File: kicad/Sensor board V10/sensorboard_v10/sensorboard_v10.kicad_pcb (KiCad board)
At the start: 2 copper layers, 100 x 100 mm, 88 parts, among them J1 Conn_01x02, J10 Conn_01x04, J11 Conn_01x02, J12 Conn_01x03, J13 Conn_01x03, J14 Conn_01x03, J15 Conn_01x03, J16 Conn_01x03, J17 Conn_01x03, J18 Conn_01x03, J19 Conn_01x03, J2 USB_C_Receptacle_USB2.0_14P, J3 Conn_01x02, J4 Conn_01x02, J5 Conn_01x02, J6 Conn_01x04, J7 Conn_01x04, J8 Conn_01x02, J9 Conn_01x02, Q1 MMBT3904, Q2 MMBT3904, SW1 SW_SPST, SW2 SW_SPST, U1 ESP32-S3-WROOM-2, U2 CH340C, U3 TJA1051T-3, U4 LM2576S-5, U5 AMS1117-3.3, U6 LM324

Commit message: Sensor Board V10 schematics
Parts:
- added C22: 100nF, RMC_Capacitor:C_0805_2012Metric_Pad1.18x1.45mm_HandSolder_L, F.Cu at (128.0, 121.8)
- added C23: 100nF, RMC_Capacitor:C_0805_2012Metric_Pad1.18x1.45mm_HandSolder_L, F.Cu at (131.0, 121.8)
- added C24: 100nF, RMC_Capacitor:C_0805_2012Metric_Pad1.18x1.45mm_HandSolder_L, F.Cu at (134.0, 121.8)
- added C25: 100nF, RMC_Capacitor:C_0805_2012Metric_Pad1.18x1.45mm_HandSolder_L, F.Cu at (137.0, 121.8)
- added C26: 100nF, RMC_Capacitor:C_0805_2012Metric_Pad1.18x1.45mm_HandSolder_L, F.Cu at (260.8, 122.8)
- added C27: 100nF, RMC_Capacitor:C_0805_2012Metric_Pad1.18x1.45mm_HandSolder_L, F.Cu at (260.8, 125.8)
- added C28: 100nF, RMC_Capacitor:C_0805_2012Metric_Pad1.18x1.45mm_HandSolder_L, F.Cu at (202.0, 111.8)
- added C29: 100nF, RMC_Capacitor:C_0805_2012Metric_Pad1.18x1.45mm_HandSolder_L, F.Cu at (107.0, 86.2)
- added D3: LED, RMC_LED:LED_0805_2012Metric_Pad1.45x1.40mm_HandSolder, F.Cu at (229.8, 71.8)
- added D4: LED, RMC_LED:LED_0805_2012Metric_Pad1.45x1.40mm_HandSolder, F.Cu at (229.8, 74.8)
- added J20: Conn_01x02, Connector_JST:JST_XH_B2B-XH-A_1x02_P2.50mm_Vertical, F.Cu at (196.0, 107.0)
- added J21: Conn_01x06, Connector_PinHeader_2.54mm:PinHeader_2x03_P2.54mm_Vertical, F.Cu at (237.8, 51.5)
- added R30: 5k, RMC_Resistor:R_0805_2012Metric_Pad1.20x1.40mm_HandSolder_L, F.Cu at (128.0, 127.2)
- added R31: 1k, RMC_Resistor:R_0805_2012Metric_Pad1.20x1.40mm_HandSolder_L, F.Cu at (130.9, 127.2)
- added R32: 5k, RMC_Resistor:R_0805_2012Metric_Pad1.20x1.40mm_HandSolder_L, F.Cu at (133.9, 127.2)
- added R33: 1k, RMC_Resistor:R_0805_2012Metric_Pad1.20x1.40mm_HandSolder_L, F.Cu at (136.8, 127.2)
- added R34: 5k, RMC_Resistor:R_0805_2012Metric_Pad1.20x1.40mm_HandSolder_L, F.Cu at (139.8, 127.2)
- added R35: 1k, RMC_Resistor:R_0805_2012Metric_Pad1.20x1.40mm_HandSolder_L, F.Cu at (142.7, 127.2)
- added R36: 4k7, RMC_Resistor:R_0805_2012Metric_Pad1.20x1.40mm_HandSolder_L, F.Cu at (260.7, 128.7)
- added R37: 100K, RMC_Resistor:R_0805_2012Metric_Pad1.20x1.40mm_HandSolder_L, F.Cu at (202.0, 117.7)
- added R38: 330R, RMC_Resistor:R_0805_2012Metric_Pad1.20x1.40mm_HandSolder_L, F.Cu at (222.1, 69.6)
- added R39: 120R, RMC_Resistor:R_0805_2012Metric_Pad1.20x1.40mm_HandSolder_L, F.Cu at (222.1, 72.6)
- added U7: TXS0102DCU, Package_SO:VSSOP-8_2.3x2mm_P0.5mm, F.Cu at (52.0, 118.0)
- R24, R25, R26, R27: footprint RMC_Resistor:R_0805_2012Metric_Pad1.20x1.40mm_HandSolder_L -> RMC_Resistor:R_1206_3216Metric_Pad1.30x1.75mm_HandSolder_RMC
- U1: footprint RF_Module:ESP32-S3-WROOM-2 -> to be sorted:ESP32-WROOM-S3-2
- U2: footprint Package_SO:SOIC-16_3.9x9.9mm_P1.27mm -> RMC_SO:SOIC-16_3.9x9.9mm_P1.27mm_Handsolder
- moved R21 209.1 mm to (222.3, 144.7)
- moved R22 209.1 mm to (222.3, 147.6)
- moved C20 209.1 mm to (227.7, 144.7)
- moved J19 209.1 mm to (223.0, 138.8)
- moved C17 188.6 mm to (230.0, 120.4)
- moved J16 188.6 mm to (225.2, 114.5)
- moved R15 188.6 mm to (224.5, 120.4)
- moved R16 188.6 mm to (224.5, 123.4)
- moved C3 136.7 mm to (183.8, 64.2)
- moved R24 122.7 mm to (133.6, 134.8), turned to 90 degrees
- moved J4 120.4 mm to (135.5, 143.5), turned to 90 degrees
- moved R25 118.5 mm to (136.5, 134.8), turned to 90 degrees
- moved R26 114.4 mm to (139.5, 134.8), turned to 90 degrees
- moved R27 110.2 mm to (142.5, 134.8), turned to 90 degrees
- moved J5 109.4 mm to (143.3, 143.5), turned to 90 degrees
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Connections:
- net /voltage divider/3.3V_INPUT renamed POT1_IN
- net /voltage divider1/3.3V_INPUT renamed POT2_IN
- net /voltage divider2/3.3V_INPUT renamed POT3_IN
- net /voltage divider3/3.3V_INPUT renamed POT4_IN
- net /voltage divider4/3.3V_INPUT renamed APPS_5V_IN
- net /voltage divider5/3.3V_INPUT renamed BRAKE_IN
- net /voltage divider6/3.3V_INPUT renamed FLOW_IN
- C13 pad 2: /voltage divider/1.65V OUTPUT -> POT1_OUT
- C14 pad 2: /voltage divider1/1.65V OUTPUT -> POT2_OUT
- C15 pad 2: /voltage divider2/1.65V OUTPUT -> POT3_OUT
- C16 pad 2: /voltage divider3/1.65V OUTPUT -> POT4_OUT
- C17 pad 2: /voltage divider4/1.65V OUTPUT -> APPS_5V_OUT
- C18 pad 2: /voltage divider5/1.65V OUTPUT -> BRAKE_OUT
- C19 pad 2: /voltage divider6/1.65V OUTPUT -> FLOW_OUT
- J19 pad 3: +5V -> +3.3V
- R10 pad 2: /voltage divider1/1.65V OUTPUT -> POT2_OUT
- R11 pad 2: /voltage divider2/1.65V OUTPUT -> POT3_OUT
- R12 pad 2: /voltage divider2/1.65V OUTPUT -> POT3_OUT
- R13 pad 2: /voltage divider3/1.65V OUTPUT -> POT4_OUT
- R14 pad 2: /voltage divider3/1.65V OUTPUT -> POT4_OUT
- R15 pad 2: /voltage divider4/1.65V OUTPUT -> APPS_5V_OUT
- R16 pad 2: /voltage divider4/1.65V OUTPUT -> APPS_5V_OUT
- R17 pad 2: /voltage divider5/1.65V OUTPUT -> BRAKE_OUT
- R18 pad 2: /voltage divider5/1.65V OUTPUT -> BRAKE_OUT
- R19 pad 2: /voltage divider6/1.65V OUTPUT -> FLOW_OUT
- R20 pad 2: /voltage divider6/1.65V OUTPUT -> FLOW_OUT
- R7 pad 2: /voltage divider/1.65V OUTPUT -> POT1_OUT
- R8 pad 2: /voltage divider/1.65V OUTPUT -> POT1_OUT
- R9 pad 2: /voltage divider1/1.65V OUTPUT -> POT2_OUT
- U1 pad 10: unconnected-(U1-IO17-Pad10) -> BRAKE_TEMP_OUT3
- U1 pad 11: unconnected-(U1-IO18-Pad11) -> BRAKE_TEMP_OUT4
- U1 pad 12: unconnected-(U1-IO8-Pad12) -> BRAKE_OUT
- U1 pad 13: unconnected-(U1-USB_D-/IO19-Pad13) -> CAN_RX
- U1 pad 14: unconnected-(U1-USB_D+/IO20-Pad14) -> CAN_TX
- U1 pad 15: LVB_S -> LVB_TEMP
- U1 pad 17: unconnected-(U1-IO9-Pad17) -> PUMP_THERMISTOR_IN
- U1 pad 18: unconnected-(U1-IO10-Pad18) -> LVB_S
- U1 pad 19: unconnected-(U1-IO11-Pad19) -> MOSI
- U1 pad 20: unconnected-(U1-IO12-Pad20) -> SCK
- U1 pad 21: unconnected-(U1-IO13-Pad21) -> MISO
- U1 pad 22: unconnected-(U1-IO14-Pad22) -> FLOW_OUT
- U1 pad 23: unconnected-(U1-IO21-Pad23) -> SDA
- U1 pad 31: unconnected-(U1-IO38-Pad31) -> SCL
- U1 pad 8: unconnected-(U1-IO15-Pad8) -> BRAKE_TEMP_OUT1
- U1 pad 9: unconnected-(U1-IO16-Pad9) -> BRAKE_TEMP_OUT2
- U6 pad 13: BRAKE_TEMP_OUT4 -> Net-(U6D--)
- U6 pad 6: BRAKE_TEMP_OUT3 -> Net-(U6B--)
- U6 pad 9: BRAKE_TEMP_OUT2 -> Net-(U6C--)

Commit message: Sensor Board v10
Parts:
- removed J1: Conn_01x02, Connector_JST:JST_VH_B2P-VH_1x02_P3.96mm_Vertical
- added C30: 100nF, RMC_Capacitor:C_0805_2012Metric_Pad1.18x1.45mm_HandSolder_L, B.Cu at (183.2, 131.6)
- added C31: 100nF, RMC_Capacitor:C_0805_2012Metric_Pad1.18x1.45mm_HandSolder_L, B.Cu at (188.1, 135.4)
- added C32: 22uF, RMC_Capacitor:C_0805_2012Metric_Pad1.18x1.45mm_HandSolder_L, F.Cu at (126.2, 143.0)
- added C33: 22uF, RMC_Capacitor:C_0805_2012Metric_Pad1.18x1.45mm_HandSolder_L, F.Cu at (116.2, 143.0)
- added C34: 100nF, RMC_Capacitor:C_0805_2012Metric_Pad1.18x1.45mm_HandSolder_L, F.Cu at (129.6, 143.0)
- added C35: 100nF, RMC_Capacitor:C_0805_2012Metric_Pad1.18x1.45mm_HandSolder_L, F.Cu at (113.4, 143.0)
- added D5: SMA Diode, Diode_SMD:D_SMA_Handsoldering, F.Cu at (107.6, 134.4)
- added J22: Conn_01x02, Connector_JST:JST_XH_B2B-XH-A_1x02_P2.50mm_Vertical, F.Cu at (151.3, 144.3)
- added J23: Conn_01x03, Connector_JST:JST_XH_B3B-XH-A_1x03_P2.50mm_Vertical, F.Cu at (191.7, 106.3)
- added J24: Conn_01x01, Connector_PinHeader_2.54mm:PinHeader_1x01_P2.54mm_Vertical, F.Cu at (158.0, 82.4)
- added J25: Conn_01x04, Connector_JST:JST_XH_B4B-XH-A_1x04_P2.50mm_Vertical, F.Cu at (189.2, 91.7)
- added J26: Conn_01x03, Connector_JST:JST_XH_B3B-XH-A_1x03_P2.50mm_Vertical, F.Cu at (158.2, 141.8)
- added J27: Conn_01x03, Connector_JST:JST_XH_B3B-XH-A_1x03_P2.50mm_Vertical, F.Cu at (165.2, 141.9)
- added L2: 4.7-22uH, RMC_Inductor:L_10.4x10.4_H4.8, F.Cu at (121.0, 134.4)
- added R40: 4k7, RMC_Resistor:R_0805_2012Metric_Pad1.20x1.40mm_HandSolder_L, B.Cu at (154.7, 145.7)
- added R41: 5k1, RMC_Resistor:R_0805_2012Metric_Pad1.20x1.40mm_HandSolder_L, B.Cu at (196.2, 68.6)
- added R42: 5k1, RMC_Resistor:R_0805_2012Metric_Pad1.20x1.40mm_HandSolder_L, B.Cu at (196.2, 65.6)
- added R43: 499R, RMC_Resistor:R_0805_2012Metric_Pad1.20x1.40mm_HandSolder_L, F.Cu at (181.8, 64.0)
- added R44: 680R, RMC_Resistor:R_0805_2012Metric_Pad1.20x1.40mm_HandSolder_L, F.Cu at (123.6, 148.0)
- added U8: 74LVC1G17, Package_TO_SOT_SMD:SOT-23-5_HandSoldering, B.Cu at (182.4, 134.8)
- added U9: MT3608/SDB628, Package_TO_SOT_SMD:SOT-23-6_Handsoldering, F.Cu at (121.0, 143.2)
- C17, C20, C3, R1, R10, R11, R12, R13, R14, R15, R16, R17, R18, R19, R2, R20, R21, R22, R24, R25, R26, R27, R3, R37, R7, R8, R9: moved to B.Cu
- C2: moved to F.Cu
- J21: value Conn_01x06 -> Conn_01x02; footprint Connector_PinHeader_2.54mm:PinHeader_2x03_P2.54mm_Vertical -> Connector_JST:JST_XH_B2B-XH-A_1x02_P2.50mm_Vertical
- R23: value 499R -> 249k
- moved R23 153.3 mm to (118.2, 148.0)
- moved R1 136.0 mm to (162.3, 145.7), turned to 90 degrees
- moved C27 118.6 mm to (145.3, 98.7), turned to 180 degrees
- moved C26 118.5 mm to (145.3, 96.1)
- moved J10 111.5 mm to (150.6, 118.2)
- moved J6 111.5 mm to (150.6, 103.6)
- moved J7 111.5 mm to (150.6, 110.9)
- moved R36 106.1 mm to (159.4, 97.4)
- moved U7 102.5 mm to (152.5, 97.7), turned to 180 degrees
- moved C20 100.4 mm to (171.6, 61.4)
- moved D3 99.0 mm to (131.2, 80.4), turned to 180 degrees
- moved R38 91.3 mm to (131.2, 78.2), turned to 180 degrees
- moved J18 87.7 mm to (185.9, 141.8), turned to -90 degrees
- moved R20 87.1 mm to (188.1, 137.7), turned to 180 degrees
- moved C17 85.0 mm to (171.6, 58.6)
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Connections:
- C28 pad 1: PUMP_THERMISTOR_IN -> PUMP_THERM_IN
- J2 pad A5: unconnected-(J2-CC1-PadA5) -> Net-(J2-CC1)
- J2 pad B5: unconnected-(J2-CC2-PadB5) -> Net-(J2-CC2)
- J20 pad 1: PUMP_THERMISTOR_IN -> PUMP_THERM_IN
- J21 pad 1: MISO -> CAN+
- J21 pad 2: +5V -> CAN-
- J4 pad 1: GND -> BRAKE_TEMP1
- J4 pad 2: BRAKE_TEMP1 -> +24V
- J5 pad 1: GND -> BRAKE_TEMP2
- J5 pad 2: BRAKE_TEMP2 -> +24V
- J8 pad 1: GND -> BRAKE_TEMP3
- J8 pad 2: BRAKE_TEMP3 -> +24V
- J9 pad 1: GND -> BRAKE_TEMP4
- J9 pad 2: BRAKE_TEMP4 -> +24V
- R19 pad 2: FLOW_OUT -> Net-(C31-Pad2)
- R20 pad 2: FLOW_OUT -> Net-(C31-Pad2)
- R23 pad 1: USB_RX -> +24V
- R23 pad 2: Net-(U1-TXD0/IO43) -> Net-(U9-FB)
- R24 pad 1: GND -> GND2
- R25 pad 1: GND -> GND2
- R26 pad 1: GND -> GND2
- R27 pad 1: GND -> GND2
- R28 pad 1: Net-(U6A--) -> Net-(U6B--)
- R29 pad 2: Net-(U6A--) -> Net-(U6B--)
- R30 pad 1: Net-(U6C--) -> Net-(U6A--)
- R31 pad 2: Net-(U6C--) -> Net-(U6A--)
- R32 pad 1: Net-(U6B--) -> Net-(U6D--)
- R33 pad 2: Net-(U6B--) -> Net-(U6D--)
- R34 pad 1: Net-(U6D--) -> Net-(U6C--)
- R35 pad 2: Net-(U6D--) -> Net-(U6C--)
- R37 pad 1: PUMP_THERMISTOR_IN -> PUMP_THERM_IN
- U1 pad 12: BRAKE_OUT -> SDA_3V3
- U1 pad 13: CAN_RX -> IO19
- U1 pad 14: CAN_TX -> IO20
- U1 pad 15: LVB_TEMP -> Temp_sensor
- U1 pad 16: unconnected-(U1-IO46-Pad16) -> IO46
- U1 pad 17: PUMP_THERMISTOR_IN -> SCL_3V3
- U1 pad 19: MOSI -> LVB_TEMP
- U1 pad 20: SCK -> BRAKE_OUT
- U1 pad 21: MISO -> PUMP_THERM_IN
- U1 pad 23: SDA -> CAN_RX
- U1 pad 24: unconnected-(U1-IO47-Pad24) -> IO47
- U1 pad 25: unconnected-(U1-IO48-Pad25) -> IO48
- U1 pad 26: unconnected-(U1-IO45-Pad26) -> IO45
- U1 pad 31: SCL -> CAN_TX
- U1 pad 32: unconnected-(U1-MTCK/IO39-Pad32) -> IO39
- U1 pad 33: unconnected-(U1-MTDO/IO40-Pad33) -> IO40
- U1 pad 34: unconnected-(U1-MTDI/IO41-Pad34) -> IO41
- U1 pad 35: unconnected-(U1-MTMS/IO42-Pad35) -> IO42
- U1 pad 37: Net-(U1-TXD0/IO43) -> USB_RX
- U2 pad 3: USB_RX -> Net-(U2-RXD)
- U6 pad 1: BRAKE_TEMP_OUT1 -> BRAKE_TEMP_OUT2
- U6 pad 10: BRAKE_TEMP2 -> BRAKE_TEMP4
- U6 pad 12: BRAKE_TEMP4 -> BRAKE_TEMP3
- U6 pad 14: BRAKE_TEMP_OUT4 -> BRAKE_TEMP_OUT3
- U6 pad 3: BRAKE_TEMP1 -> BRAKE_TEMP2
- U6 pad 5: BRAKE_TEMP3 -> BRAKE_TEMP1
- U6 pad 7: BRAKE_TEMP_OUT3 -> BRAKE_TEMP_OUT1
- U6 pad 8: BRAKE_TEMP_OUT2 -> BRAKE_TEMP_OUT4
- U7 pad 1: SDA -> SCL
- U7 pad 4: SDA_3V3 -> SCL_3V3
- U7 pad 5: SCL_3V3 -> SDA_3V3
- U7 pad 8: SCL -> SDA
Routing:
- net +24V: track 0.00 -> 54.9 mm
- net BRAKE_TEMP4: track 0.00 -> 37.1 mm
- net BRAKE_TEMP3: track 0.00 -> 32.3 mm
- net BRAKE_TEMP1: track 0.00 -> 29.5 mm
- net BRAKE_TEMP2: track 0.00 -> 27.1 mm
- net BRAKE_TEMP_OUT3: track 0.00 -> 22.0 mm
- net BRAKE_TEMP_OUT1: track 0.00 -> 20.9 mm
- net POT3_OUT: track 0.00 -> 20.1 mm
- net POT1_OUT: track 0.00 -> 18.8 mm
- net +12V: track 26.1 -> 44.7 mm
- net BRAKE_TEMP_OUT4: track 0.00 -> 16.5 mm
- net BRAKE_TEMP_OUT2: track 0.00 -> 15.7 mm
- net Net-(D5-K): track 0.00 -> 15.3 mm
- net POT4_OUT: track 0.00 -> 14.9 mm
- net POT2_OUT: track 0.00 -> 13.6 mm
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- added copper zone on B.Cu, net GND2
- added copper zone on F.Cu, net GND2

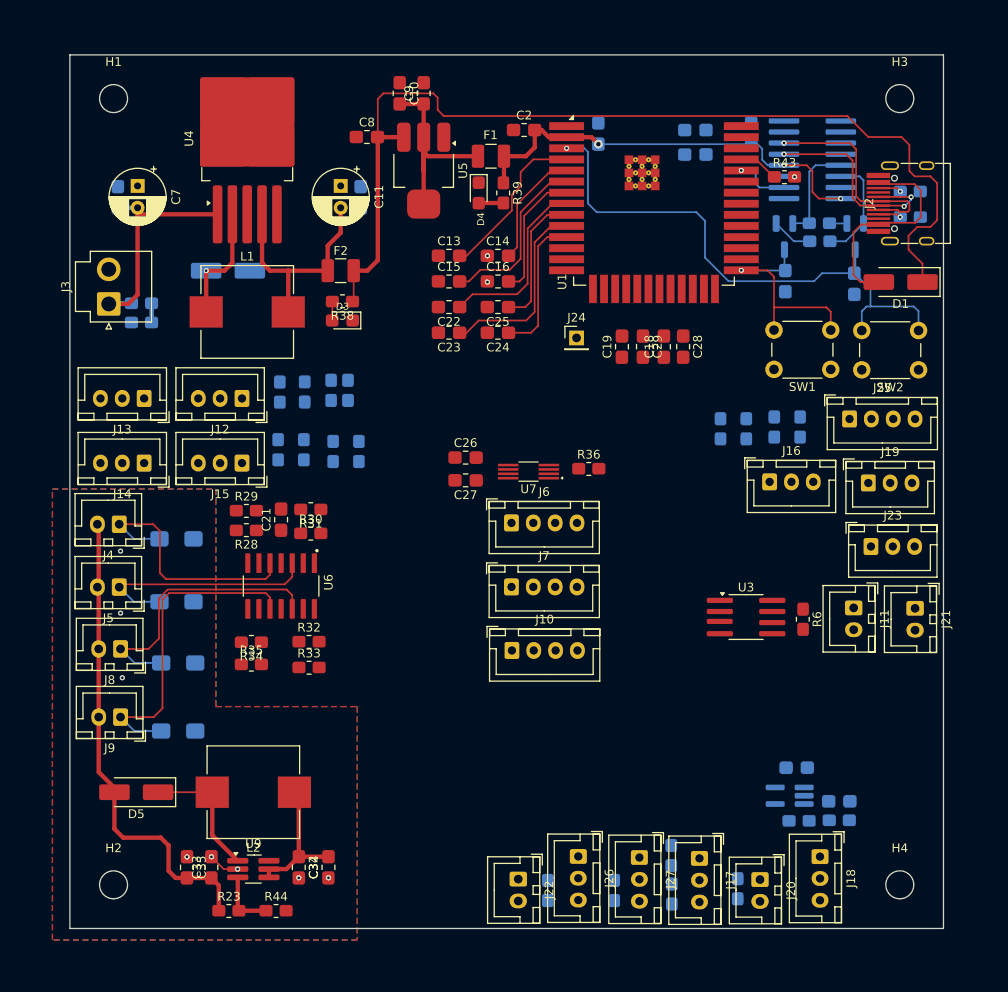
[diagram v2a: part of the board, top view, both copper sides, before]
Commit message: Sensor Board V10.0 done
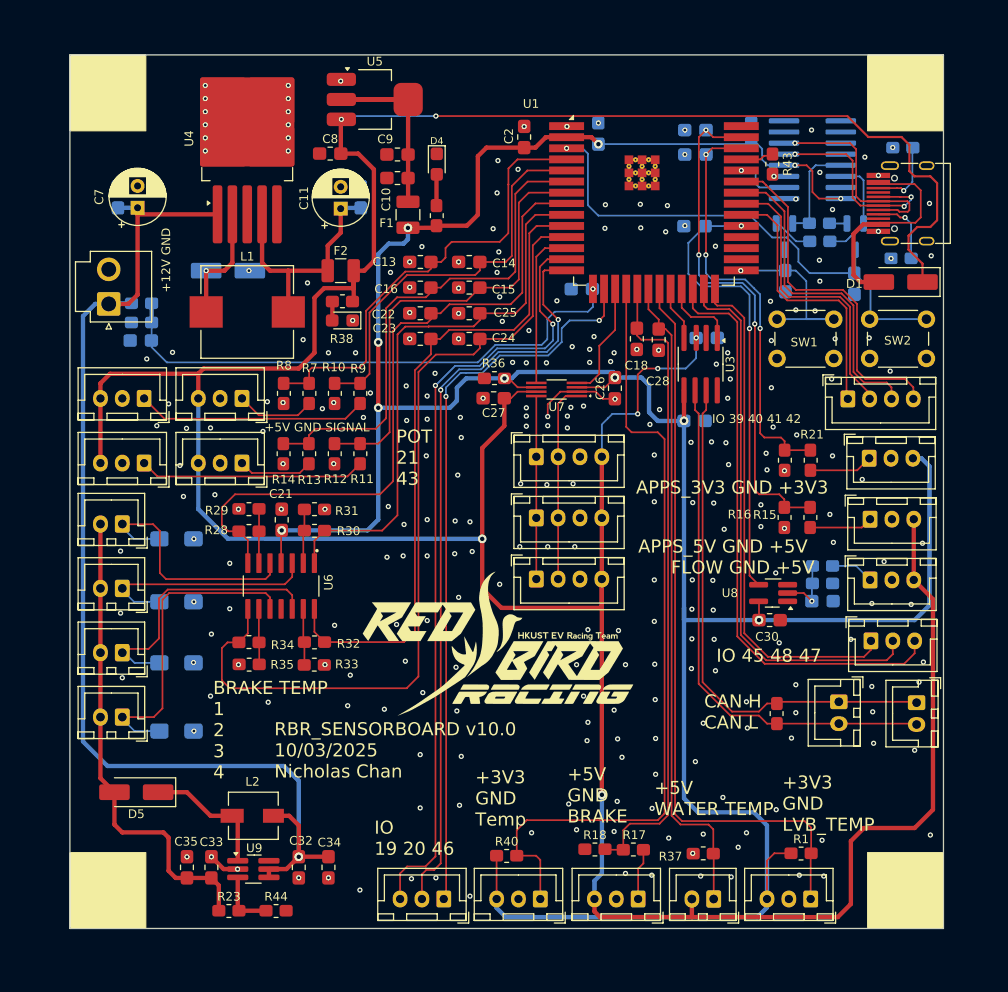
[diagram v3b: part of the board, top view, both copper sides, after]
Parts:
- removed J22: Conn_01x02, Connector_JST:JST_XH_B2B-XH-A_1x02_P2.50mm_Vertical
- removed J24: Conn_01x01, Connector_PinHeader_2.54mm:PinHeader_1x01_P2.54mm_Vertical
- added C36: 100nF, RMC_Capacitor:C_0805_2012Metric_Pad1.18x1.45mm_HandSolder_L, B.Cu at (172.9, 82.4)
- added C37: 100nF, RMC_Capacitor:C_0805_2012Metric_Pad1.18x1.45mm_HandSolder_L, B.Cu at (171.5, 91.9)
- added C38: 100nF, RMC_Capacitor:C_0805_2012Metric_Pad1.18x1.45mm_HandSolder_L, B.Cu at (108.1, 82.7)
- added G***: LOGO, RBR_logo:RBR_logo, F.Cu at (149.3, 117.3)
- added J1: Conn_01x03, Connector_JST:JST_XH_B3B-XH-A_1x03_P2.50mm_Vertical, F.Cu at (142.8, 146.6)
- C19, C29: moved to B.Cu
- C30, R1, R10, R11, R12, R13, R14, R15, R16, R17, R18, R21, R22, R37, R40, R7, R8, R9, U8: moved to F.Cu
- L2: footprint RMC_Inductor:L_10.4x10.4_H4.8 -> Inductor_SMD:L_Wuerth_HCI-5040
- moved J18 32.2 mm to (191.6, 110.1), turned to 0 degrees
- moved U3 29.4 mm to (172.2, 85.4), turned to -90 degrees
- moved R19 29.2 mm to (186.2, 108.5), turned to 180 degrees
- moved R20 27.2 mm to (186.2, 110.5)
- moved U8 23.3 mm to (180.5, 111.6)
- moved C31 23.0 mm to (186.2, 112.5)
- moved R1 21.8 mm to (183.7, 141.4), turned to 0 degrees
- moved J27 20.2 mm to (184.8, 146.6), turned to 180 degrees
- moved C26 18.8 mm to (162.4, 88.2), turned to 90 degrees
- moved C30 17.2 mm to (180.1, 114.7)
- moved C19 16.1 mm to (171.5, 69.6), turned to 0 degrees
- moved R36 15.0 mm to (148.6, 87.0), turned to 180 degrees
- moved R15 12.5 mm to (184.8, 102.9)
- moved R16 12.5 mm to (181.8, 102.9)
- moved J16 12.3 mm to (191.6, 103.2)
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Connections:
- C11 pad 1: GND -> Net-(U4-FB)
- C11 pad 2: Net-(U4-FB) -> GND
- C15 pad 2: POT3_OUT -> POT4_OUT
- C16 pad 2: POT4_OUT -> POT3_OUT
- C32 pad 2: GND2 -> GND
- C33 pad 2: GND2 -> GND
- C34 pad 1: GND2 -> GND
- C35 pad 1: GND2 -> GND
- C7 pad 1: GND -> +12V
- C7 pad 2: +12V -> GND
- J14 pad 1: POT3_IN -> POT4_IN
- J15 pad 1: POT4_IN -> POT3_IN
- J23 pad 1: IO47 -> IO45
- J23 pad 3: IO45 -> IO47
- R11 pad 1: POT3_IN -> POT4_IN
- R11 pad 2: POT3_OUT -> POT4_OUT
- R12 pad 2: POT3_OUT -> POT4_OUT
- R13 pad 1: POT4_IN -> POT3_IN
- R13 pad 2: POT4_OUT -> POT3_OUT
- R14 pad 2: POT4_OUT -> POT3_OUT
- R24 pad 1: GND2 -> GND
- R25 pad 1: GND2 -> GND
- R26 pad 1: GND2 -> GND
- R27 pad 1: GND2 -> GND
- R44 pad 2: GND2 -> GND
- U1 pad 15: Temp_sensor -> LVB_S
- U1 pad 18: LVB_S -> Temp_sensor
- U1 pad 19: LVB_TEMP -> BRAKE_OUT
- U1 pad 20: BRAKE_OUT -> PUMP_THERM_IN
- U1 pad 21: PUMP_THERM_IN -> LVB_TEMP
- U1 pad 22: FLOW_OUT -> CAN_RX
- U1 pad 23: CAN_RX -> CAN_TX
- U1 pad 31: CAN_TX -> FLOW_OUT
- U9 pad 2: GND2 -> GND
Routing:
- net +5V: track 113.6 -> 415.1 mm, vias 0 -> 7
- net +3.3V: track 49.4 -> 327.6 mm, vias 3 -> 11
- net Temp_sensor: track 0.00 -> 91.7 mm
- net IO19: track 0.00 -> 89.8 mm, vias 0 -> 2
- net +12V: track 44.7 -> 131.8 mm, vias 0 -> 1
- net IO20: track 0.00 -> 87.0 mm, vias 0 -> 2
- net LVB_TEMP: track 0.00 -> 85.3 mm
- net IO46: track 0.00 -> 84.1 mm, vias 0 -> 2
- net BRAKE_TEMP_OUT4: track 16.5 -> 97.2 mm
- net PUMP_THERM_IN: track 0.00 -> 75.3 mm
- net BRAKE_OUT: track 0.00 -> 73.5 mm
- net IO47: track 0.00 -> 67.5 mm
- net IO48: track 0.00 -> 63.2 mm
- net CAN-: track 0.00 -> 60.6 mm
- net LVB_S: track 2.20 -> 62.3 mm, vias 0 -> 1
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- removed copper zone on B.Cu, net GND2
- removed copper zone on F.Cu, net GND2
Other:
- board text added: "+12V GND"
- board text added: "+3V3 GND LVB_TEMP"
- board text added: "+3V3 GND Temp"
- board text added: "+5V GND BRAKE"
- board text added: "+5V GND SIGNAL"
- board text added: "+5V WATER TEMP"
- board text added: "APPS_3V3 GND +3V3"
- board text added: "APPS_5V GND +5V"
- board text added: "BRAKE TEMP 1 2 3 4"
- board text added: "CAN H CAN L"
- board text added: "FLOW GND +5V"
- board text added: "IO 19 20 46"
- board text added: "IO 39 40 41 42"
- board text added: "IO 45 48 47"
- board text added: "POT 21 43"
- board text added: "RBR_SENSORBOARD v10.0 10/03/2025 Nicholas Chan"

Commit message: sensor board v10
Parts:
- C13, C14, C15, C16, C22, C23, C24, C25: moved to B.Cu
- C32, C33: footprint RMC_Capacitor:C_0805_2012Metric_Pad1.18x1.45mm_HandSolder_L -> RMC_Capacitor:CP_EIA-3528-15_AVX-H_Pad1.50x2.35mm_HandSolder_RMC
- moved C36 3.10 mm to (172.9, 85.5)
- moved C35 1.60 mm to (111.8, 143.0)
- moved C32 1.48 mm to (127.5, 143.7)
- moved C33 1.14 mm to (115.1, 142.7)
- moved C34 1.11 mm to (130.7, 143.1)
- moved R40 0.70 mm to (150.0, 141.0)
- moved R1 0.53 mm to (183.7, 140.9)
- moved R37 0.50 mm to (172.5, 140.9)
- moved R18 0.16 mm to (159.9, 141.0)
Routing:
- net +12V: track 131.8 -> 134.5 mm
- net POT2_IN: track 26.5 -> 28.5 mm
- net POT4_IN: track 26.0 -> 27.8 mm
- net POT1_IN: track 9.10 -> 10.4 mm
- net POT3_IN: track 8.57 -> 9.79 mm
- net GND: track 17.9 -> 18.9 mm, vias 273 -> 215
- net +3.3V: track 327.6 -> 328.5 mm
- net POT2_OUT: track 46.0 -> 46.7 mm, vias 0 -> 1
- net BRAKE_TEMP_OUT4: track 97.2 -> 96.6 mm, vias 0 -> 1
- net +5V: track 415.1 -> 415.6 mm
- net POT1_OUT: track 52.7 -> 53.2 mm, vias 0 -> 1
- net BRAKE_TEMP_OUT2: track 64.7 -> 64.3 mm, vias 0 -> 1
- net BRAKE_TEMP_OUT1: track 77.8 -> 77.4 mm, vias 0 -> 1
- net POT3_OUT: track 58.3 -> 58.0 mm, vias 0 -> 1
- net BRAKE_TEMP_OUT3: vias 0 -> 1
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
